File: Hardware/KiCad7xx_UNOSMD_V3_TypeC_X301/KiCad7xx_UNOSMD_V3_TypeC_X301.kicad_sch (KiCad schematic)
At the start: 77 parts, among them J1 -, J2 PINHD-1X18, J3 USB_C_Receptacle_USB2.0JAE_DX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, T1 FDN340P, U1 MC33269ST, U2 LP2985-XXDBVR, U3 ATMEGA16U2, U4 ATMEGAXX8-MUR, U5 LMV358?MM, X1 POWERSUPPLY_DC21MMX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

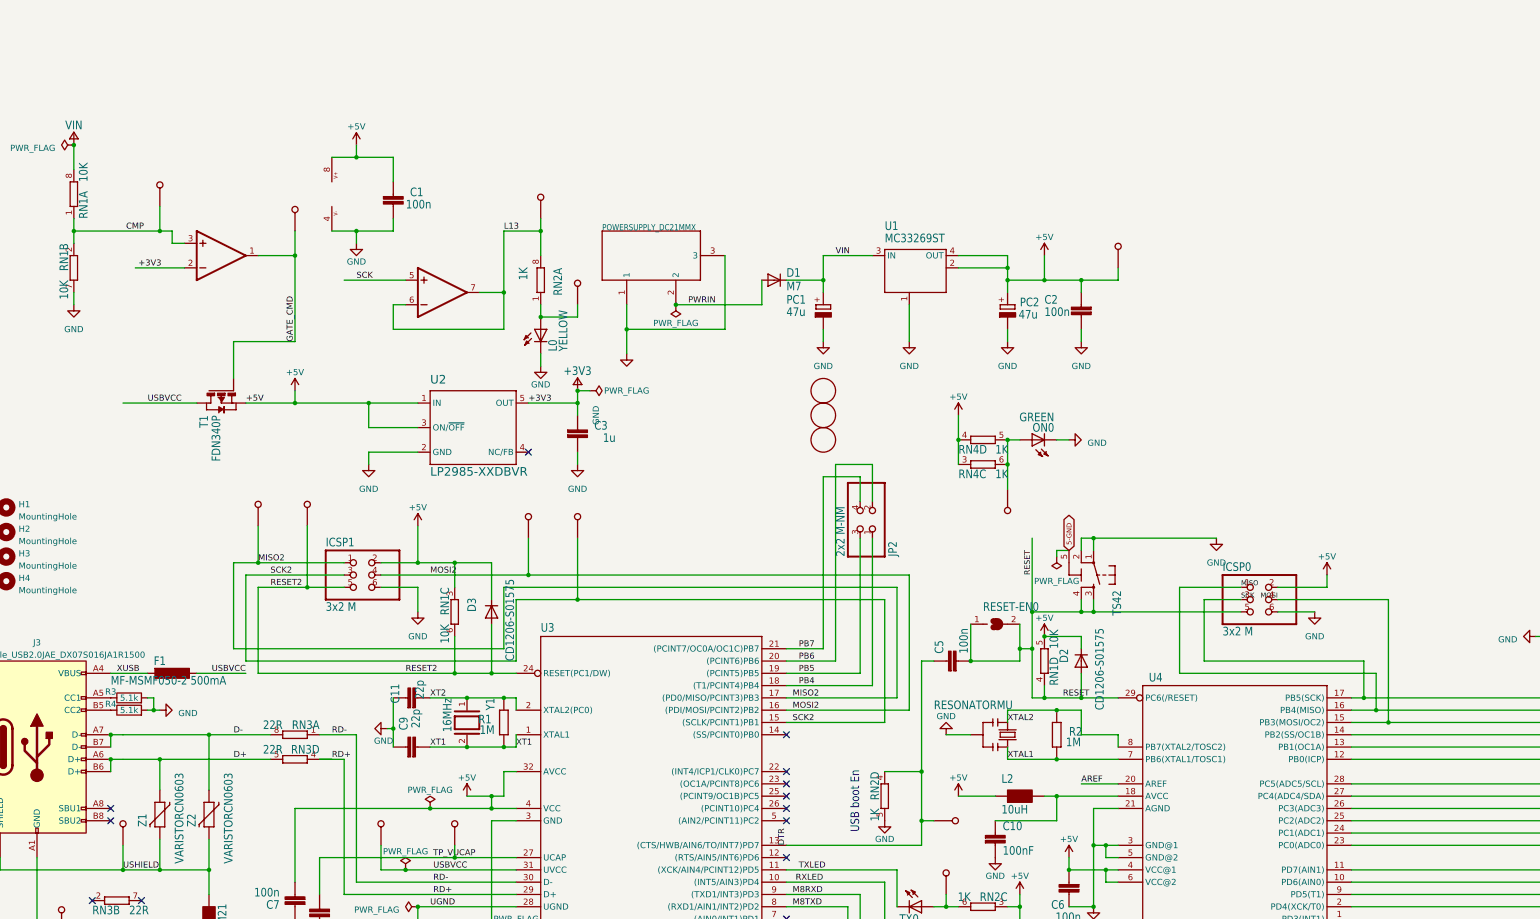
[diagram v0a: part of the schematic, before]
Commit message: Add: 回路ブロックを編集しやすいように分割
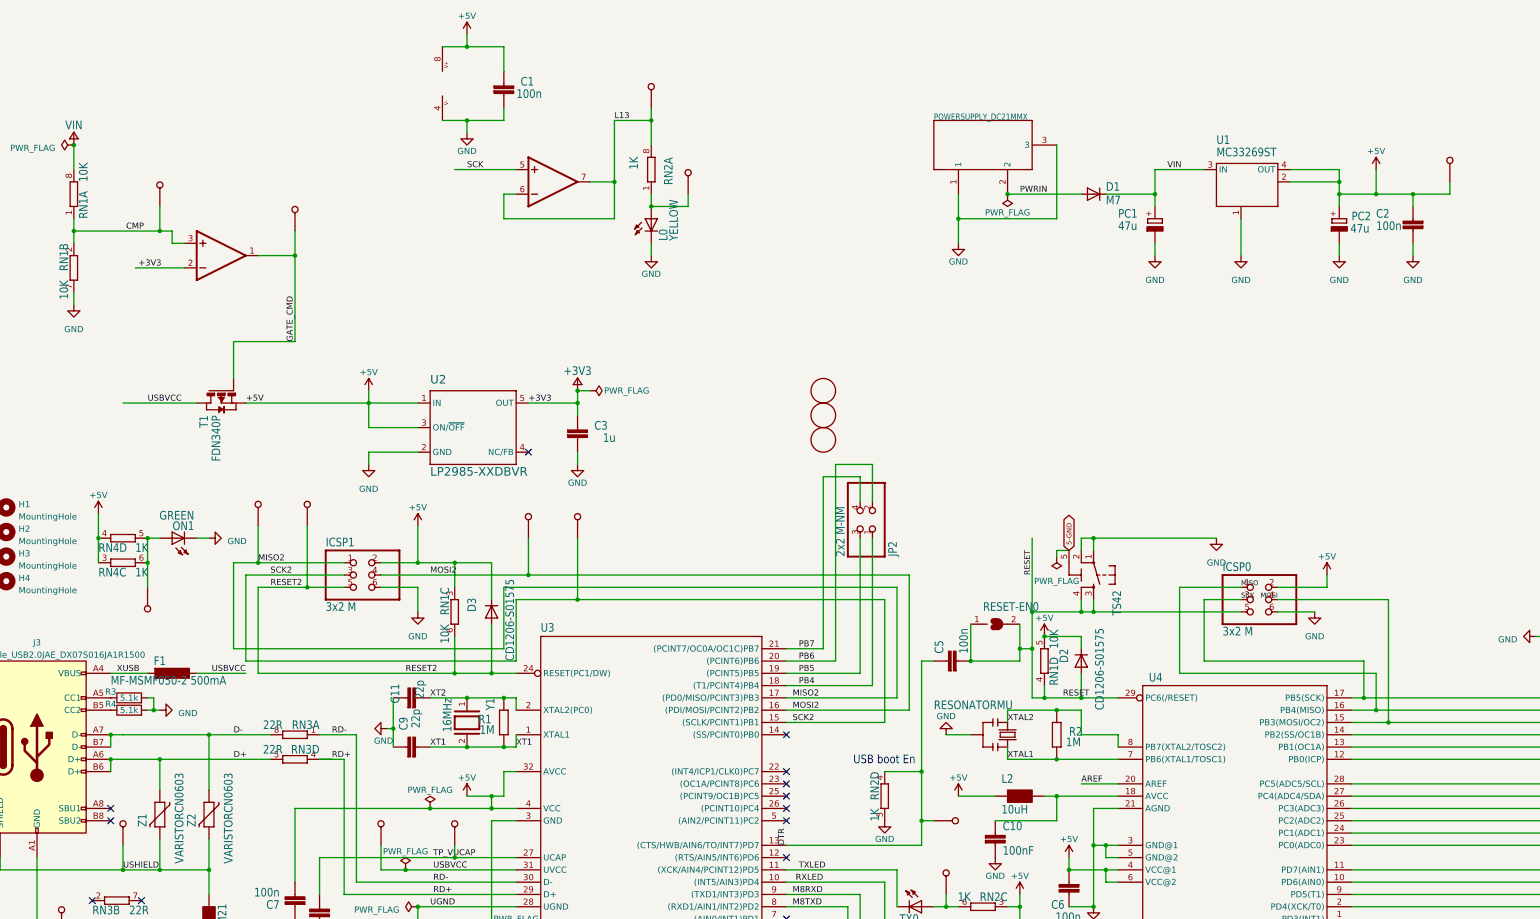
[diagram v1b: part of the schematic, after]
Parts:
- removed ON0: GREEN, UNOSMD_V3:CHIP-LED0805, symbol UNOSMD_V3-eagle-import:LEDCHIP-LED0805
- removed TP_ONL0: TP_SP, UNOSMD_V3:TP-SP, symbol UNOSMD_V3-eagle-import:TP_SP
- added ON1: GREEN, UNOSMD_V3:CHIP-LED0805, symbol UNOSMD_V3-eagle-import:LEDCHIP-LED0805
- added TP_ONL1: TP_SP, UNOSMD_V3:TP-SP, symbol UNOSMD_V3-eagle-import:TP_SP
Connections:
- net GND: now also ON1.C
- net at RN4.5 (2), RN4.6 (2): now also ON1.A, TP_ONL1.X (TESTP)
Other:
- moved on the sheet: C1, C2, D1, L0, PC1, PC2, RN2A, U1

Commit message: Add: X301の回路図に理想ダイオード回路を追加しました
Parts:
- removed L0: YELLOW, UNOSMD_V3:CHIP-LED0805, symbol UNOSMD_V3-eagle-import:LEDCHIP-LED0805
- removed TP_CMP0, TP_GATE0, TP_LCMD0, TP_LL0: TP_SP, UNOSMD_V3:TP-SP, symbol UNOSMD_V3-eagle-import:TP_SP
- added L3: YELLOW, UNOSMD_V3:CHIP-LED0805, symbol UNOSMD_V3-eagle-import:LEDCHIP-LED0805
- added R5: 47k, Resistor_SMD:R_0603_1608Metric_Pad0.98x0.95mm_HandSolder, symbol Device:R
- added TP_LCMD1, TP_LL1: TP_SP, UNOSMD_V3:TP-SP, symbol UNOSMD_V3-eagle-import:TP_SP
- added U6: BCM857BS, BCM857BS_SOT-363:SOT65P210X110-6N, symbol Nexperia_TRANSISTOR_BCM857BS_SOT-363_Component:BCM857BS__1
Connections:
- net +3V3: no longer U5.2 (-IN)
- net +5V: now also U6.4
- net GND: now also RN1.1, L3.C, R5.2; no longer RN1.7 (2)
- net L13: now also TP_LCMD1.X (TESTP)
- net USBVCC: now also U6.1
- net VIN: no longer RN1.8 (2)
- net at RN2.1: now also L3.A, TP_LL1.X (TESTP)
- removed net CMP: RN1.1, RN1.2 (1), U5.3 (+IN)
- net GATE_CMD: no longer names the net of T1.3 (G)
- net GATE_CMD: now also R5.1, U6.3; no longer U5.1 (OUT)
- new net: RN1.8 (2), U6.2, U6.5, U6.6
- no-connect marks 20 -> 25
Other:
- note added: "3V3"
- note added: "5V"
- note added: "BCM857BS"
- note added: "D13Pin LED"
- note added: "LMV358IDGKR"
- note added: "Power Block"
- note added: "Power LED"
- note added: "理想ダイオード"

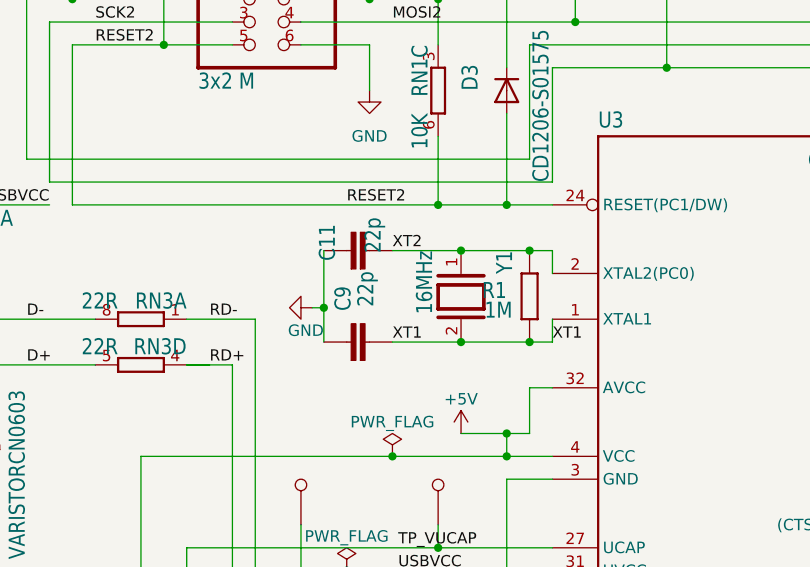
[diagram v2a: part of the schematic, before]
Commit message: Add:部品点数を減らすために16U2のクリスタルを変更
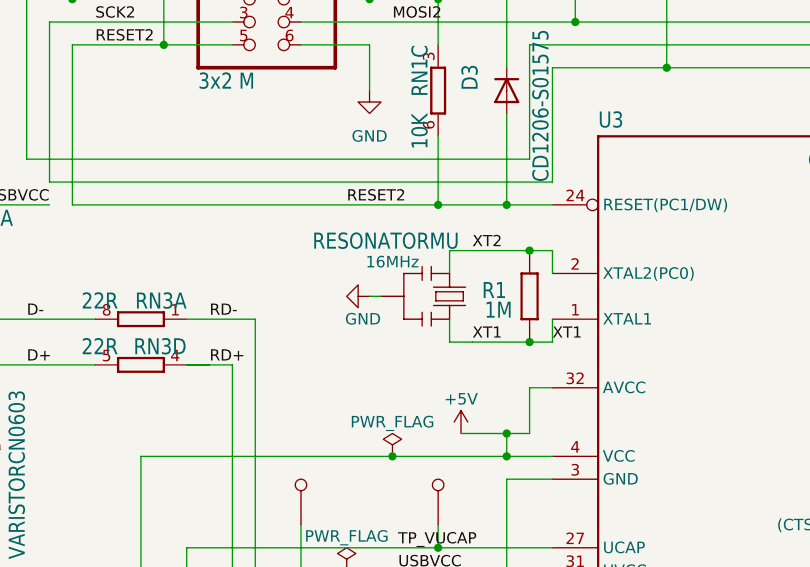
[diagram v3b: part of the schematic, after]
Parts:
- removed C11, C9: 22p, UNOSMD_V3:C0603-ROUND, symbol UNOSMD_V3-eagle-import:C-EU0603-RND
- removed Y1: 16MHz, UNOSMD_V3:QS, symbol UNOSMD_V3-eagle-import:XTAL/S
- added Y1: RESONATORMU, UNOSMD_V3:RESONATOR, symbol UNOSMD_V3-eagle-import:RESONATORMU
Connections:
- net GND: now also Y1.2
- net XT1: now also Y1.3
- net XT2: now also Y1.1
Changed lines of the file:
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@@
   (junction (at 66.04 116.84) (diameter 0) (color 0 0 0 0)
   )
-  (junction (at 109.22 154.94) (diameter 0) (color 0 0 0 0)
-  )
   (junction (at 238.76 175.26) (diameter 0) (color 0 0 0 0)
   )
@@
   (junction (at 33.02 72.39) (diameter 0) (color 0 0 0 0)
   )
-  (junction (at 93.98 151.13) (diameter 0) (color 0 0 0 0)
-  )
   (junction (at 355.6 58.42) (diameter 0) (color 0 0 0 0)
   )
@@
   (junction (at 223.52 134.62) (diameter 0) (color 0 0 0 0)
   )
-  (junction (at 109.22 144.78) (diameter 0) (color 0 0 0 0)
-  )
   (junction (at 158.75 43.18) (diameter 0) (color 0 0 0 0)
   )
@@
     (stroke (width 0.1524) (type solid))
   )
+  (wire (pts (xy 107.95 144.78) (xy 107.95 147.32))
+    (stroke (width 0) (type default))
+  )
   (wire (pts (xy 292.1 144.78) (xy 294.64 144.78))
     (stroke (width 0.1524) (type solid))
@@
     (stroke (width 0.1524) (type solid))
   )
-  (wire (pts (xy 92.71 151.13) (xy 93.98 151.13))
+  (wire (pts (xy 99.06 149.86) (xy 100.33 149.86))
     (stroke (width 0) (type default))
   )
@@
     (stroke (width 0.1524) (type solid))
   )
-  (wire (pts (xy 109.22 144.78) (xy 101.6 144.78))
+  (wire (pts (xy 110.49 144.78) (xy 116.84 144.78))
     (stroke (width 0.1524) (type solid))
   )
@@
     (stroke (width 0.1524) (type solid))
   )
-  (wire (pts (xy 109.22 144.78) (xy 116.84 144.78))
-    (stroke (width 0.1524) (type solid))
-  )
   (wire (pts (xy 360.68 73.66) (xy 360.68 57.15))
     (stroke (width 0.1524) (type solid))
@@
     (stroke (width 0.1524) (type solid))
   )
+  (wire (pts (xy 107.95 152.4) (xy 107.95 154.94))
+    (stroke (width 0) (type default))
+  )
   (wire (pts (xy 187.96 213.36) (xy 187.96 187.96))
     (stroke (width 0.1524) (type solid))
@@
     (stroke (width 0.1524) (type solid))
   )
+  (wire (pts (xy 107.95 154.94) (xy 110.49 154.94))
+    (stroke (width 0) (type default))
+  )
   (wire (pts (xy 45.72 157.48) (xy 45.72 163.83))
     (stroke (width 0.1524) (type solid))
@@
     (stroke (width 0.1524) (type solid))
   )
-  (wire (pts (xy 109.22 154.94) (xy 101.6 154.94))
+  (wire (pts (xy 110.49 154.94) (xy 116.84 154.94))
     (stroke (width 0.1524) (type solid))
   )
@@
     (stroke (width 0.1524) (type solid))
   )
+  (wire (pts (xy 110.49 144.78) (xy 107.95 144.78))
+    (stroke (width 0) (type default))
+  )
   (wire (pts (xy 243.84 167.64) (xy 238.76 167.64))
     (stroke (width 0.1524) (type solid))
@@
     (stroke (width 0.1524) (type solid))
   )
-  (wire (pts (xy 93.98 151.13) (xy 93.98 154.94))
-    (stroke (width 0.1524) (type solid))
-  )
   (wire (pts (xy 223.52 134.62) (xy 226.06 134.62))
     (stroke (width 0.1524) (type solid))
@@
     (stroke (width 0.1524) (type solid))
   )
-  (wire (pts (xy 116.84 154.94) (xy 109.22 154.94))
-    (stroke (width 0.1524) (type solid))
-  )
   (bus (pts (xy 368.3 167.64) (xy 368.3 170.18))
     (stroke (width 0.762) (type solid))
@@
     (stroke (width 0.1524) (type solid))
   )
-  (wire (pts (xy 93.98 144.78) (xy 93.98 151.13))
-    (stroke (width 0.1524) (type solid))
-  )
   (wire (pts (xy 187.96 187.96) (xy 175.26 187.96))
     (stroke (width 0.1524) (type solid))
@@
     (effects (font (size 1.2446 1.2446)) (justify left bottom))
   )
-  (label "XT2" (at 101.6 144.78 0) (fields_autoplaced)
+  (label "XT2" (at 110.49 144.78 0) (fields_autoplaced)
     (effects (font (size 1.2446 1.2446)) (justify left bottom))
   )
@@
     (effects (font (size 1.2446 1.2446)) (justify left bottom))
   )
-  (label "XT1" (at 101.6 154.94 0) (fields_autoplaced)
+  (label "XT1" (at 110.49 154.94 0) (fields_autoplaced)
     (effects (font (size 1.2446 1.2446)) (justify left bottom))
   )
@@
     )
   )
-  (symbol (lib_id "UNOSMD_V3-eagle-import:C-EU0603-RND") (at 99.06 154.94 270) (mirror x) (unit 1)
-    (in_bom yes) (on_board yes) (dnp no)
-    (property "Reference" "C9" (at 97.155 148.717 0)
-      (effects (font (size 1.778 1.5113)) (justify right top))
-    )
-    (property "Value" "22p" (at 99.695 147.066 0)
-      (effects (font (size 1.778 1.5113)) (justify right top))
-    )
-    (property "Footprint" "UNOSMD_V3:C0603-ROUND" (at 99.06 154.94 0)
-      (effects (font (size 1.27 1.27)) hide)
-    )
-    (property "Datasheet" "" (at 99.06 154.94 0)
-      (effects (font (size 1.27 1.27)) hide)
-    )
-    (pin "1")
-    (pin "2")
-    (instances
-      (project "KiCad7xx_UNOSMD_V3_TypeC_X301"
-        (path "/d0e6deaf-1f53-4aef-8d1c-efd362921a61"
-          (reference "C9") (unit 1)
-        )
-      )
-    )
-  )
   (symbol (lib_id "power:GND") (at 77.47 82.55 0) (unit 1)
     (in_bom yes) (on_board yes) (dnp no) (fields_autoplaced)
@@
     )
   )
-  (symbol (lib_id "UNOSMD_V3-eagle-import:C-EU0603-RND") (at 99.06 144.78 270) (mirror x) (unit 1)
-    (in_bom yes) (on_board yes) (dnp no)
-    (property "Reference" "C11" (at 93.345 145.923 0)
-      (effects (font (size 1.778 1.5113)) (justify left bottom))
-    )
-    (property "Value" "22p" (at 98.425 145.034 0)
-      (effects (font (size 1.778 1.5113)) (justify left bottom))
-    )
-    (property "Footprint" "UNOSMD_V3:C0603-ROUND" (at 99.06 144.78 0)
-      (effects (font (size 1.27 1.27)) hide)
-    )
-    (property "Datasheet" "" (at 99.06 144.78 0)
-      (effects (font (size 1.27 1.27)) hide)
-    )
-    (pin "1")
-    (pin "2")
-    (instances
-      (project "KiCad7xx_UNOSMD_V3_TypeC_X301"
-        (path "/d0e6deaf-1f53-4aef-8d1c-efd362921a61"
-          (reference "C11") (unit 1)
-        )
-      )
-    )
-  )
   (symbol (lib_id "power:GND") (at 245.11 68.58 0) (unit 1)
     (in_bom yes) (on_board yes) (dnp no) (fields_autoplaced)
@@
     )
   )
+  (symbol (lib_id "UNOSMD_V3-eagle-import:RESONATORMU") (at 107.95 149.86 0) (unit 1)
+    (in_bom yes) (on_board yes) (dnp no)
+    (property "Reference" "Y1" (at 102.87 145.288 0)
+      (effects (font (size 1.778 1.5113)) (justify left bottom) hide)
+    )
+    (property "Value" "RESONATORMU" (at 92.71 144.78 0)
+      (effects (font (size 1.778 1.5113)) (justify left bottom))
+    )
+    (property "Footprint" "UNOSMD_V3:RESONATOR" (at 107.95 149.86 0)
+      (effects (font (size 1.27 1.27)) hide)
+    )
+    (property "Datasheet" "" (at 107.95 149.86 0)
+      (effects (font (size 1.27 1.27)) hide)
+    )
+    (property "値２" "16MHz" (at 101.6 146.05 0)
+      (effects (font (size 1.27 1.27)))
+    )
+    (pin "1")
+    (pin "2")
+    (pin "3")
+    (instances
+      (project "KiCad7xx_UNOSMD_V3_TypeC_X301"
+        (path "/d0e6deaf-1f53-4aef-8d1c-efd362921a61"
+          (reference "Y1") (unit 1)
+        )
+      )
+    )
+  )
   (symbol (lib_id "UNOSMD_V3-eagle-import:TP_SP") (at 236.22 215.9 270) (unit 1)
     (in_bom yes) (on_board yes) (dnp no)
@@
     )
   )
-  (symbol (lib_id "power:GND") (at 92.71 151.13 270) (unit 1)
+  (symbol (lib_id "power:GND") (at 99.06 149.86 270) (unit 1)
     (in_bom yes) (on_board yes) (dnp no)
-    (property "Reference" "#PWR03" (at 86.36 151.13 0)
+    (property "Reference" "#PWR03" (at 92.71 149.86 0)
       (effects (font (size 1.27 1.27)) hide)
     )
-    (property "Value" "GND" (at 93.98 153.67 90)
+    (property "Value" "GND" (at 100.33 152.4 90)
       (effects (font (size 1.27 1.27)) (justify right))
     )
-    (property "Footprint" "" (at 92.71 151.13 0)
+    (property "Footprint" "" (at 99.06 149.86 0)
       (effects (font (size 1.27 1.27)) hide)
     )
-    (property "Datasheet" "" (at 92.71 151.13 0)
+    (property "Datasheet" "" (at 99.06 149.86 0)
       (effects (font (size 1.27 1.27)) hide)
     )
@@
         )
       )
-    )
-  )
-  (symbol (lib_id "UNOSMD_V3-eagle-import:XTAL/S") (at 109.22 149.86 270) (unit 1)
-    (in_bom yes) (on_board yes) (dnp no)
-    (property "Reference" "Y1" (at 113.03 144.78 0)
-      (effects (font (size 1.778 1.5113)) (justify left bottom))
-    )
-    (property "Value" "16MHz" (at 104.14 144.78 0)
-      (effects (font (size 1.778 1.5113)) (justify left bottom))
-    )
-    (property "Footprint" "UNOSMD_V3:QS" (at 109.22 149.86 0)
-      (effects (font (size 1.27 1.27)) hide)
-    )
-    (property "Datasheet" "" (at 109.22 149.86 0)
-      (effects (font (size 1.27 1.27)) hide)
-    )
-    (pin "1")
-    (pin "2")
-    (instances
-      (project "KiCad7xx_UNOSMD_V3_TypeC_X301"
-        (path "/d0e6deaf-1f53-4aef-8d1c-efd362921a61"
-          (reference "Y1") (unit 1)
-        )
-      )

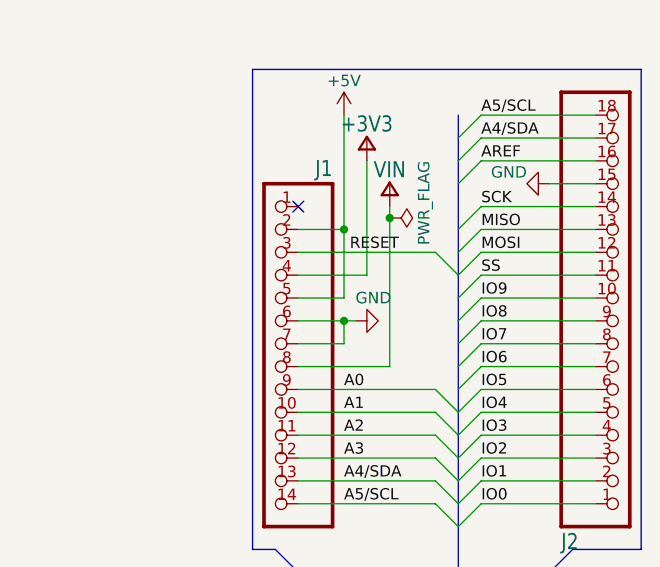
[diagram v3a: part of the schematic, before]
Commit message: Add: VIN電源にダイオードを追加
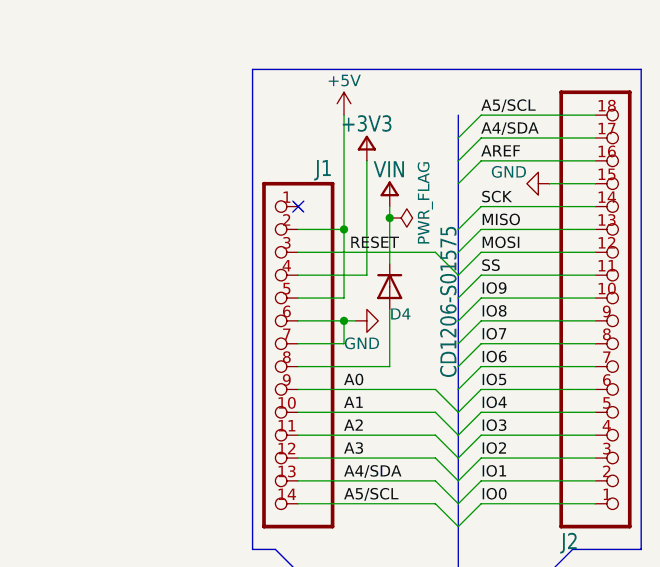
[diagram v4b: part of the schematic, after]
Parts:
- added D4: CD1206-S01575, UNOSMD_V3:MINIMELF, symbol UNOSMD_V3-eagle-import:DIODE-MINIMELF
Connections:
- net VIN: now also D4.C; no longer J1.8
- new net: D4.A, J1.8
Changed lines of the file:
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@@
     (stroke (width 0.1524) (type solid))
   )
-  (wire (pts (xy 360.68 73.66) (xy 360.68 57.15))
+  (wire (pts (xy 360.68 73.66) (xy 360.68 67.31))
     (stroke (width 0.1524) (type solid))
   )
@@
   )
   (wire (pts (xy 116.84 165.1) (xy 114.3 165.1))
+    (stroke (width 0.1524) (type solid))
+  )
+  (wire (pts (xy 360.68 62.23) (xy 360.68 57.15))
     (stroke (width 0.1524) (type solid))
   )
@@
       (effects (font (size 1.27 1.27)) hide)
     )
-    (property "Value" "GND" (at 356.87 66.04 90)
+    (property "Value" "GND" (at 355.6 71.12 90)
       (effects (font (size 1.27 1.27)) (justify right))
     )
@@
         )
       )
+    )
+  )
+  (symbol (lib_id "UNOSMD_V3-eagle-import:DIODE-MINIMELF") (at 360.68 64.77 90) (unit 1)
+    (in_bom yes) (on_board yes) (dnp no)
+    (property "Reference" "D4" (at 360.68 68.58 90)
+      (effects (font (size 1.24 1.24)) (justify right top))
+    )
+    (property "Value" "CD1206-S01575" (at 368.3 74.93 0)
+      (effects (font (size 1.778 1.5113)) (justify left bottom))
+    )
+    (property "Footprint" "UNOSMD_V3:MINIMELF" (at 360.68 64.77 0)
+      (effects (font (size 1.27 1.27)) hide)
+    )
+    (property "Datasheet" "" (at 360.68 64.77 0)
+      (effects (font (size 1.27 1.27)) hide)
+    )
+    (pin "A")
+    (pin "C")
+    (instances
+      (project "KiCad7xx_UNOSMD_V3_TypeC_X301"
+        (path "/d0e6deaf-1f53-4aef-8d1c-efd362921a61"
+          (reference "D4") (unit 1)
+        )
+      )
